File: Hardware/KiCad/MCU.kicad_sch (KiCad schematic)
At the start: 1 part, among them U2 Teensy4.1

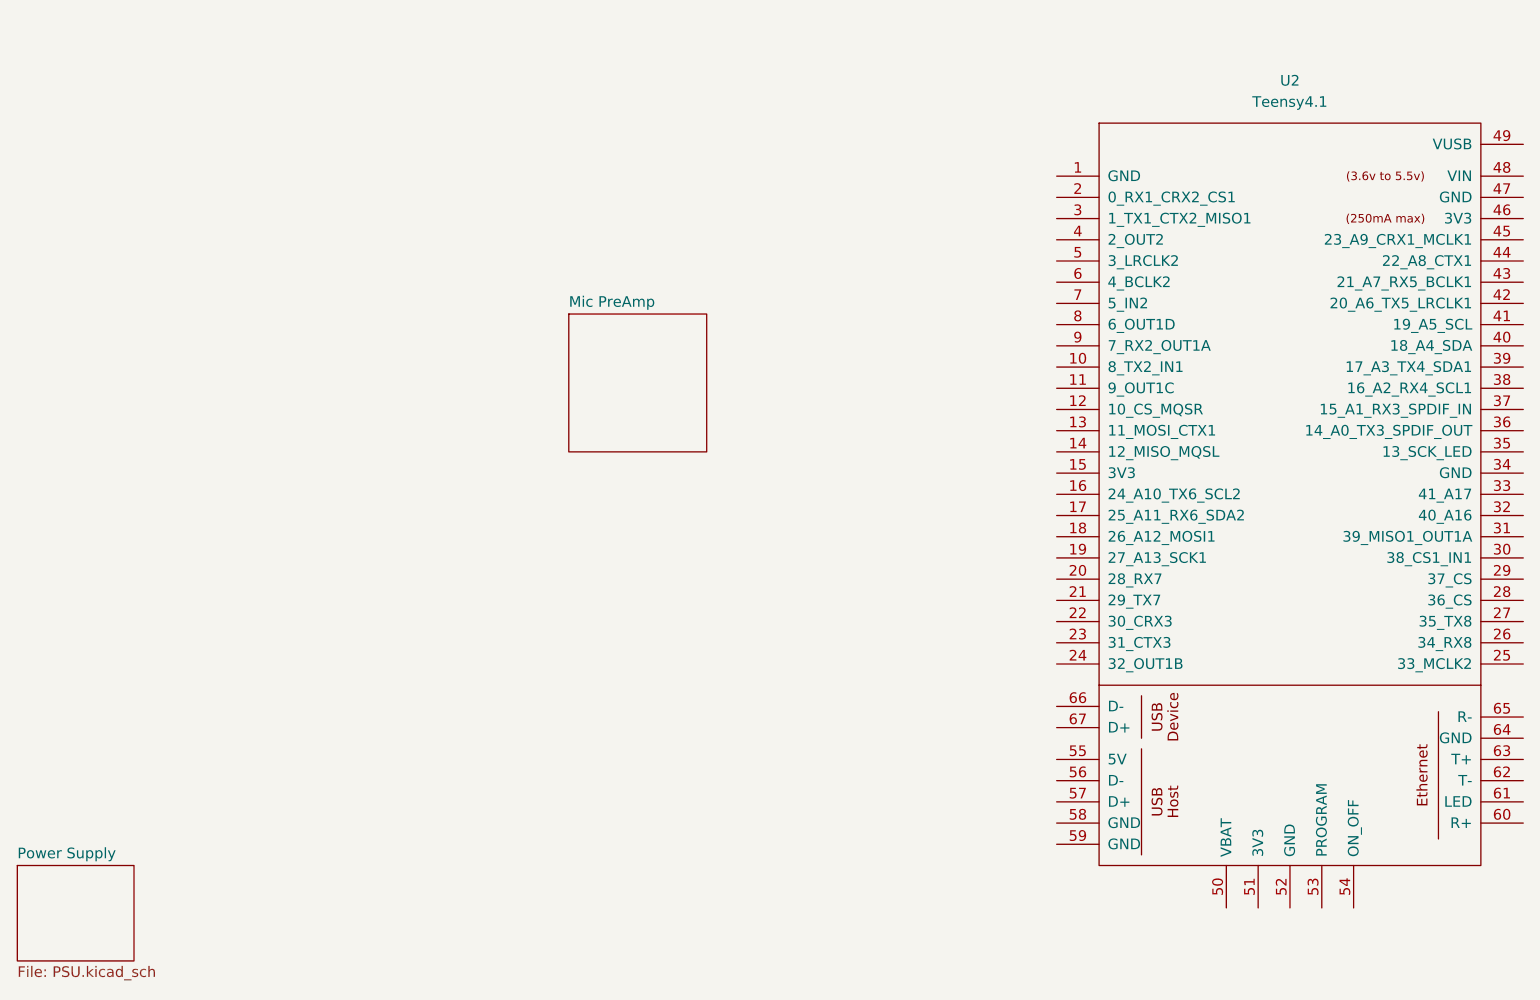
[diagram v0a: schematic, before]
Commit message: Hierarchical sheet for MCU
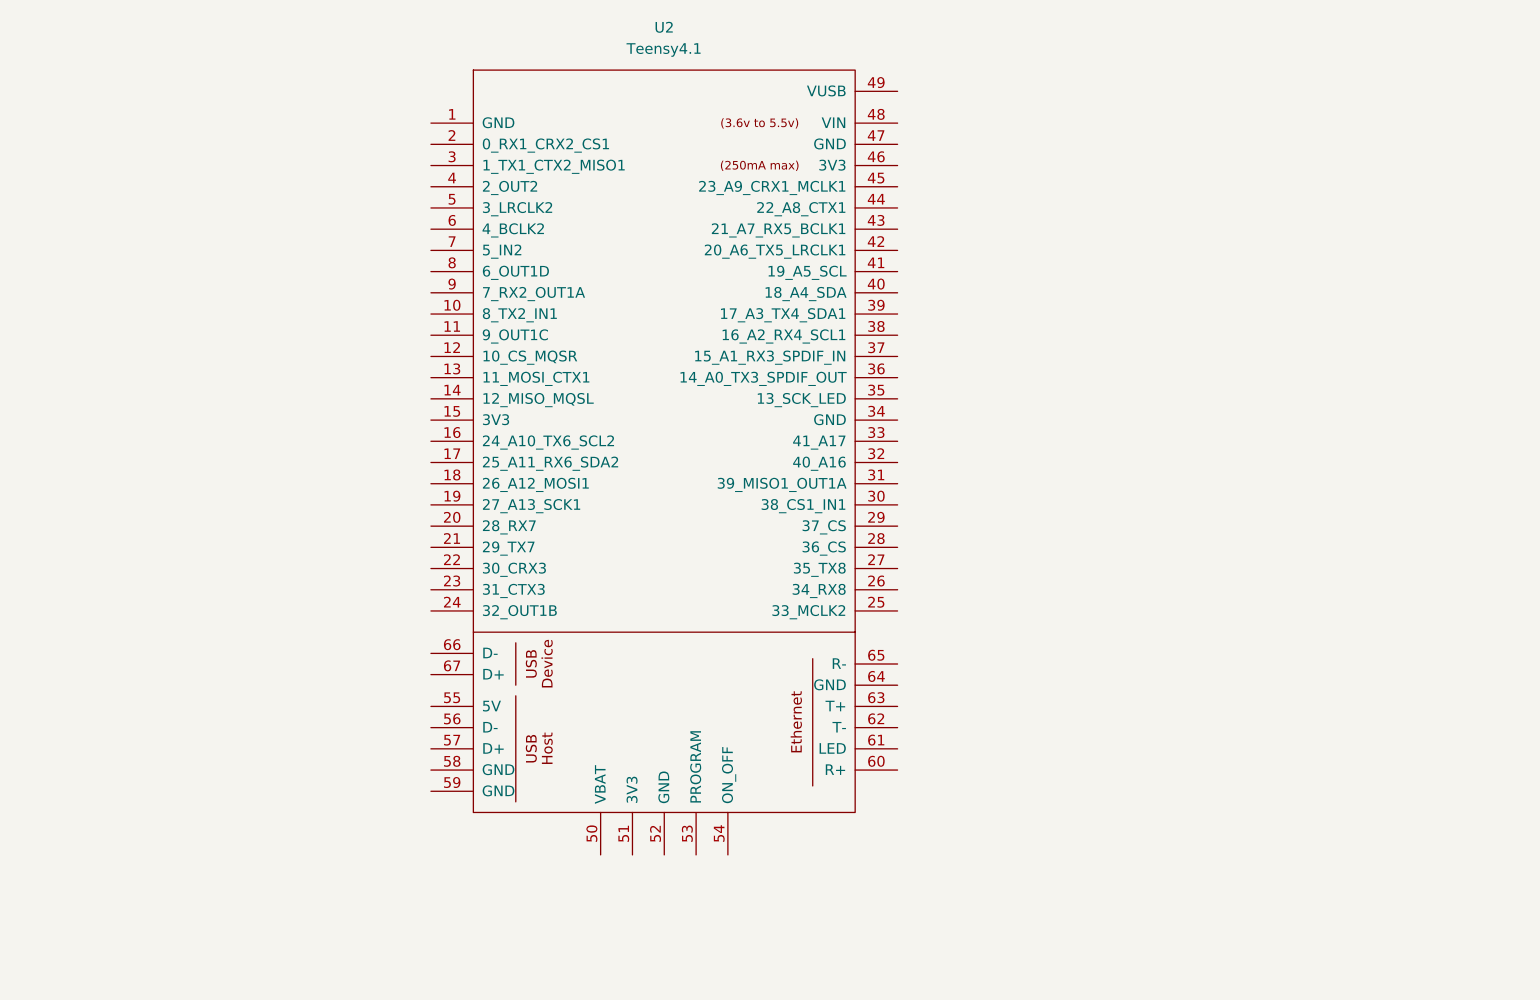
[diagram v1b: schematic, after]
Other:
- removed sheet Mic PreAmp
- removed sheet Power Supply
- title: Vocoder PCB -> (none)
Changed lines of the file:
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@@
 	(paper "A4")
 	(title_block
-		(title "Vocoder PCB")
 		(date "2025-04-03")
 		(rev "0.1")
 		(company "Sounds Like Tim")
-		(comment 1 "Tim Wannet")
 	)
 	(symbol
 		(lib_id "Teensy:Teensy4.1")
-		(at 217.17 118.11 0)
+		(at 142.24 111.76 0)
 		(unit 1)
 		(exclude_from_sim no)
@@
 		(fields_autoplaced yes)
 		(property "Reference" "U2"
-			(at 217.17 52.07 0)
+			(at 142.24 45.72 0)
 			(effects
 				(font
@@
 		)
 		(property "Value" "Teensy4.1"
-			(at 217.17 54.61 0)
+			(at 142.24 48.26 0)
 			(effects
 				(font
@@
 		)
 		(property "Footprint" ""
-			(at 207.01 107.95 0)
+			(at 132.08 101.6 0)
 			(effects
 				(font
@@
 		)
 		(property "Datasheet" ""
-			(at 207.01 107.95 0)
+			(at 132.08 101.6 0)
 			(effects
 				(font
@@
 		)
 		(property "Description" ""
-			(at 217.17 118.11 0)
+			(at 142.24 111.76 0)
 			(effects
 				(font
@@
 		)
 		(instances
-			(project ""
-				(path "/e827c80a-ca8d-4d24-8db6-878b575a1aed"
+			(project "Hardware"
+				(path "/e827c80a-ca8d-4d24-8db6-878b575a1aed/80744173-9491-4551-a74b-98f5922bdb3a"
 					(reference "U2")
 					(unit 1)
@@
 		)
 	)
-	(sheet
-		(at 64.77 146.05)
-		(size 13.97 11.43)
-		(fields_autoplaced yes)
-		(stroke
-			(width 0.1524)
-			(type solid)
-		)
-		(fill
-			(color 0 0 0 0.0000)
-		)
-		(property "Sheetname" "Power Supply"
-			(at 64.77 145.3384 0)
-			(effects
-				(font
-					(size 1.27 1.27)
-				)
-				(justify left bottom)
-			)
-		)
-		(property "Sheetfile" "PSU.kicad_sch"
-			(at 64.77 158.0646 0)
-			(effects
-				(font
-					(size 1.27 1.27)
-				)
-				(justify left top)
-			)
-		)
-		(instances
-			(project "Hardware"
-				(path "/e827c80a-ca8d-4d24-8db6-878b575a1aed"
-					(page "3")
-				)
-			)
-		)
-	)
-	(sheet
-		(at 130.81 80.01)
-		(size 16.51 16.51)
-		(fields_autoplaced yes)
-		(stroke
-			(width 0.1524)
-			(type solid)
-		)
-		(fill
-			(color 0 0 0 0.0000)
-		)
-		(property "Sheetname" "Mic PreAmp"
-			(at 130.81 79.2984 0)
-			(show_name yes)
-			(effects
-				(font
-					(size 1.27 1.27)
-				)
-				(justify left bottom)
-			)
-		)
-		(property "Sheetfile" "PreAmp.kicad_sch"
-			(at 130.81 97.1046 0)
-			(effects
-				(font
-					(size 1.27 1.27)
-				)
-				(justify left top)
-				(hide yes)
-			)
-		)
-		(instances
-			(project "Hardware"
-				(path "/e827c80a-ca8d-4d24-8db6-878b575a1aed"
-					(page "2")
-				)
-			)
-		)
-	)
-	(sheet_instances
-		(path "/"
-			(page "1")
-		)
-	)

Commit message: Re-orginanisation
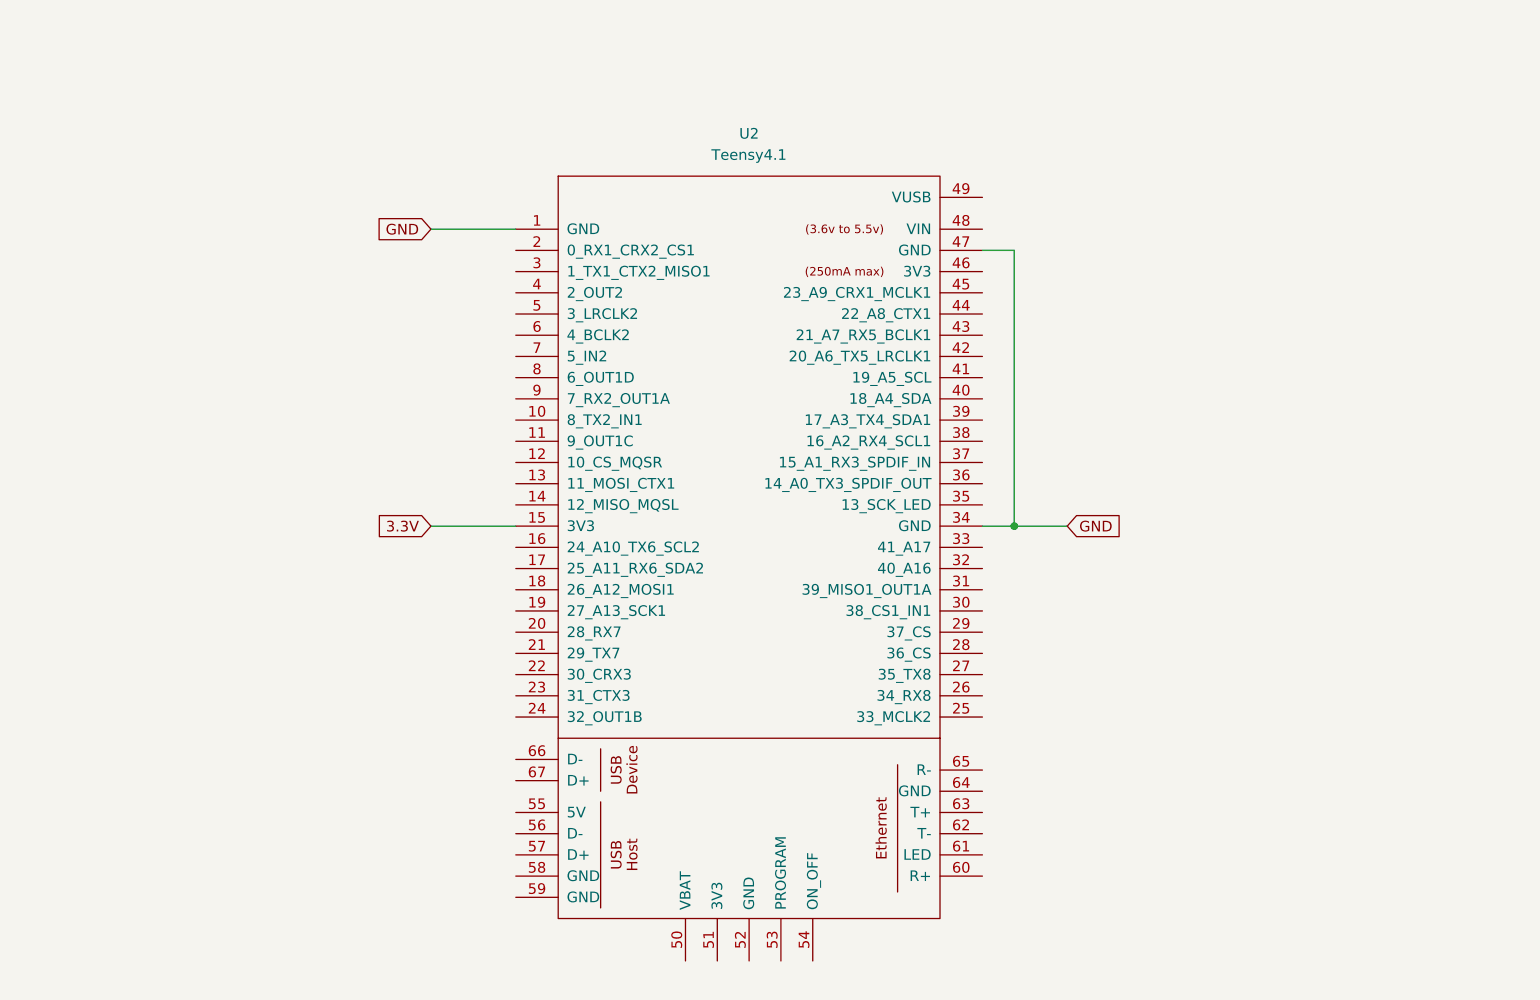
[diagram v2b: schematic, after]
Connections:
- net GND: now reaches U2.1 (GND)
- net GND: now also U2.34 (GND), U2.47 (GND)
- net 3.3V: now reaches U2.15 (3V3)
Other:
- moved on the sheet: U2
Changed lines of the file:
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@@
 (kicad_sch
-	(version 20231120)
+	(version 20250114)
 	(generator "eeschema")
-	(generator_version "8.0")
+	(generator_version "9.0")
 	(paper "A4")
 	(title_block
@@
 		(company "Sounds Like Tim")
 	)
+	(junction
+		(at 184.15 105.41)
+		(diameter 0)
+		(color 0 0 0 0)
+	)
+	(wire
+		(pts
+			(xy 184.15 105.41) (xy 190.5 105.41)
+		)
+		(stroke
+			(width 0)
+			(type default)
+		)
+	)
+	(wire
+		(pts
+			(xy 184.15 72.39) (xy 184.15 105.41)
+		)
+		(stroke
+			(width 0)
+			(type default)
+		)
+	)
+	(wire
+		(pts
+			(xy 180.34 105.41) (xy 184.15 105.41)
+		)
+		(stroke
+			(width 0)
+			(type default)
+		)
+	)
+	(wire
+		(pts
+			(xy 114.3 69.85) (xy 124.46 69.85)
+		)
+		(stroke
+			(width 0)
+			(type default)
+		)
+	)
+	(wire
+		(pts
+			(xy 114.3 105.41) (xy 124.46 105.41)
+		)
+		(stroke
+			(width 0)
+			(type default)
+		)
+	)
+	(wire
+		(pts
+			(xy 180.34 72.39) (xy 184.15 72.39)
+		)
+		(stroke
+			(width 0)
+			(type default)
+		)
+	)
+	(global_label "GND"
+		(shape input)
+		(at 190.5 105.41 0)
+		(fields_autoplaced yes)
+		(effects
+			(font
+				(size 1.27 1.27)
+			)
+			(justify left)
+		)
+		(property "Intersheetrefs" "${INTERSHEET_REFS}"
+			(at 197.3557 105.41 0)
+			(effects
+				(font
+					(size 1.27 1.27)
+				)
+				(justify left)
+				(hide yes)
+			)
+		)
+	)
+	(global_label "GND"
+		(shape input)
+		(at 114.3 69.85 180)
+		(fields_autoplaced yes)
+		(effects
+			(font
+				(size 1.27 1.27)
+			)
+			(justify right)
+		)
+		(property "Intersheetrefs" "${INTERSHEET_REFS}"
+			(at 107.4443 69.85 0)
+			(effects
+				(font
+					(size 1.27 1.27)
+				)
+				(justify right)
+				(hide yes)
+			)
+		)
+	)
+	(global_label "3.3V"
+		(shape input)
+		(at 114.3 105.41 180)
+		(fields_autoplaced yes)
+		(effects
+			(font
+				(size 1.27 1.27)
+			)
+			(justify right)
+		)
+		(property "Intersheetrefs" "${INTERSHEET_REFS}"
+			(at 107.2024 105.41 0)
+			(effects
+				(font
+					(size 1.27 1.27)
+				)
+				(justify right)
+				(hide yes)
+			)
+		)
+	)
 	(symbol
 		(lib_id "Teensy:Teensy4.1")
-		(at 142.24 111.76 0)
+		(at 152.4 124.46 0)
 		(unit 1)
 		(exclude_from_sim no)
@@
 		(fields_autoplaced yes)
 		(property "Reference" "U2"
-			(at 142.24 45.72 0)
+			(at 152.4 58.42 0)
 			(effects
 				(font
@@
 		)
 		(property "Value" "Teensy4.1"
-			(at 142.24 48.26 0)
+			(at 152.4 60.96 0)
 			(effects
 				(font
@@
 		)
 		(property "Footprint" ""
-			(at 132.08 101.6 0)
+			(at 142.24 114.3 0)
 			(effects
 				(font
@@
 		)
 		(property "Datasheet" ""
-			(at 132.08 101.6 0)
+			(at 142.24 114.3 0)
 			(effects
 				(font
@@
 		)
 		(property "Description" ""
-			(at 142.24 111.76 0)
+			(at 152.4 124.46 0)
 			(effects
 				(font
